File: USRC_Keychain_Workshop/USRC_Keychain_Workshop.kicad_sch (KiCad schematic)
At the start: 29 parts, among them U1 ICM7555xB, U2 4017

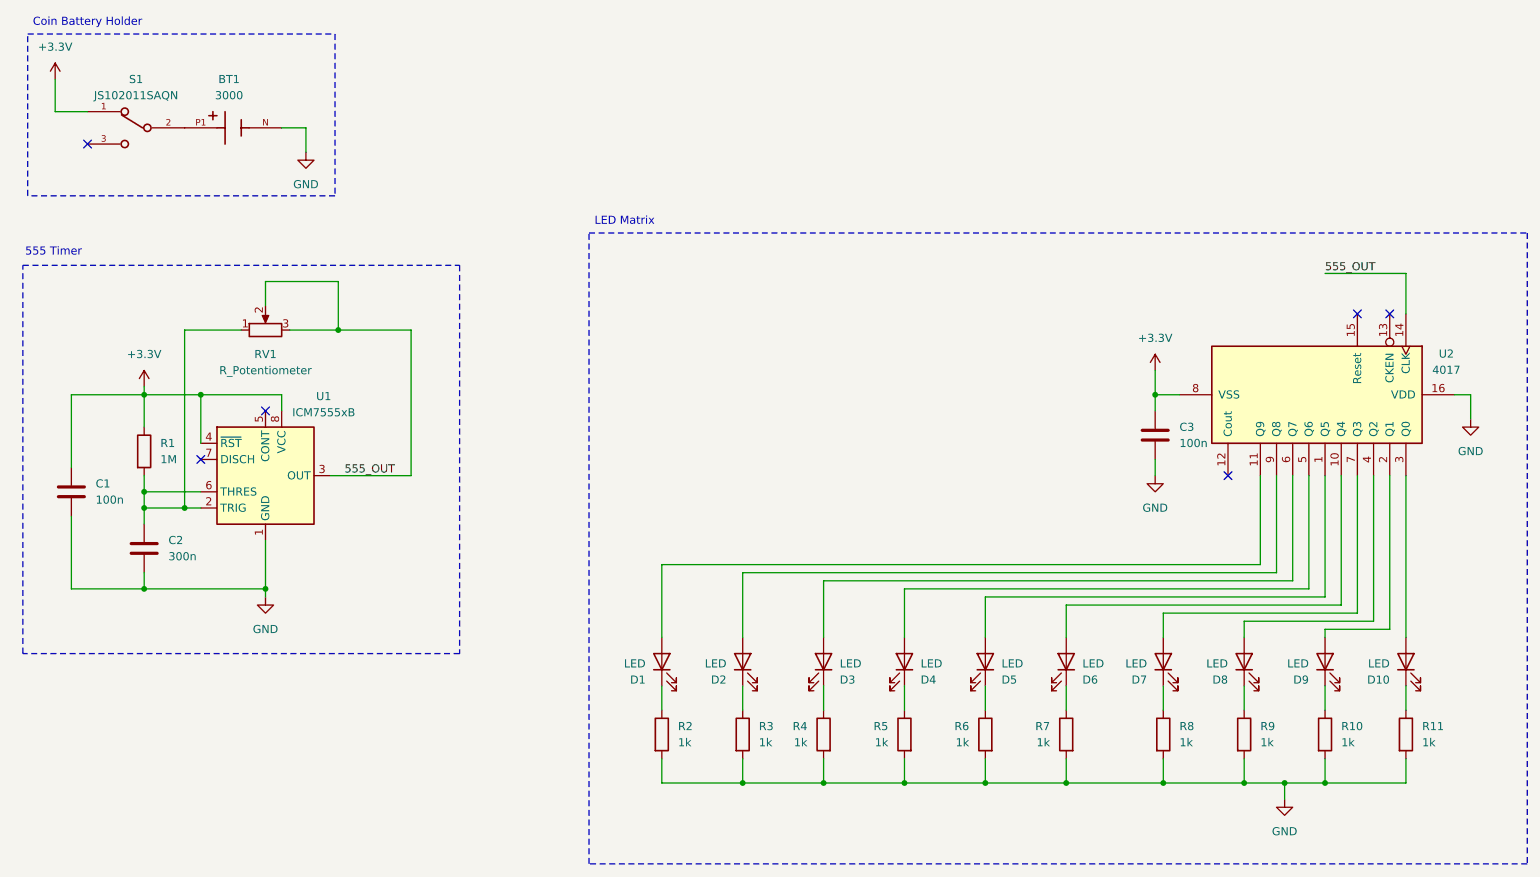
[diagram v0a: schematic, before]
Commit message: USRC_Keychain_Workshop version 2
Uploaded Version 2, a more trimmed down version of the KiCAD Keychain PCB Workshop, open the project from the KiCAD Project File.
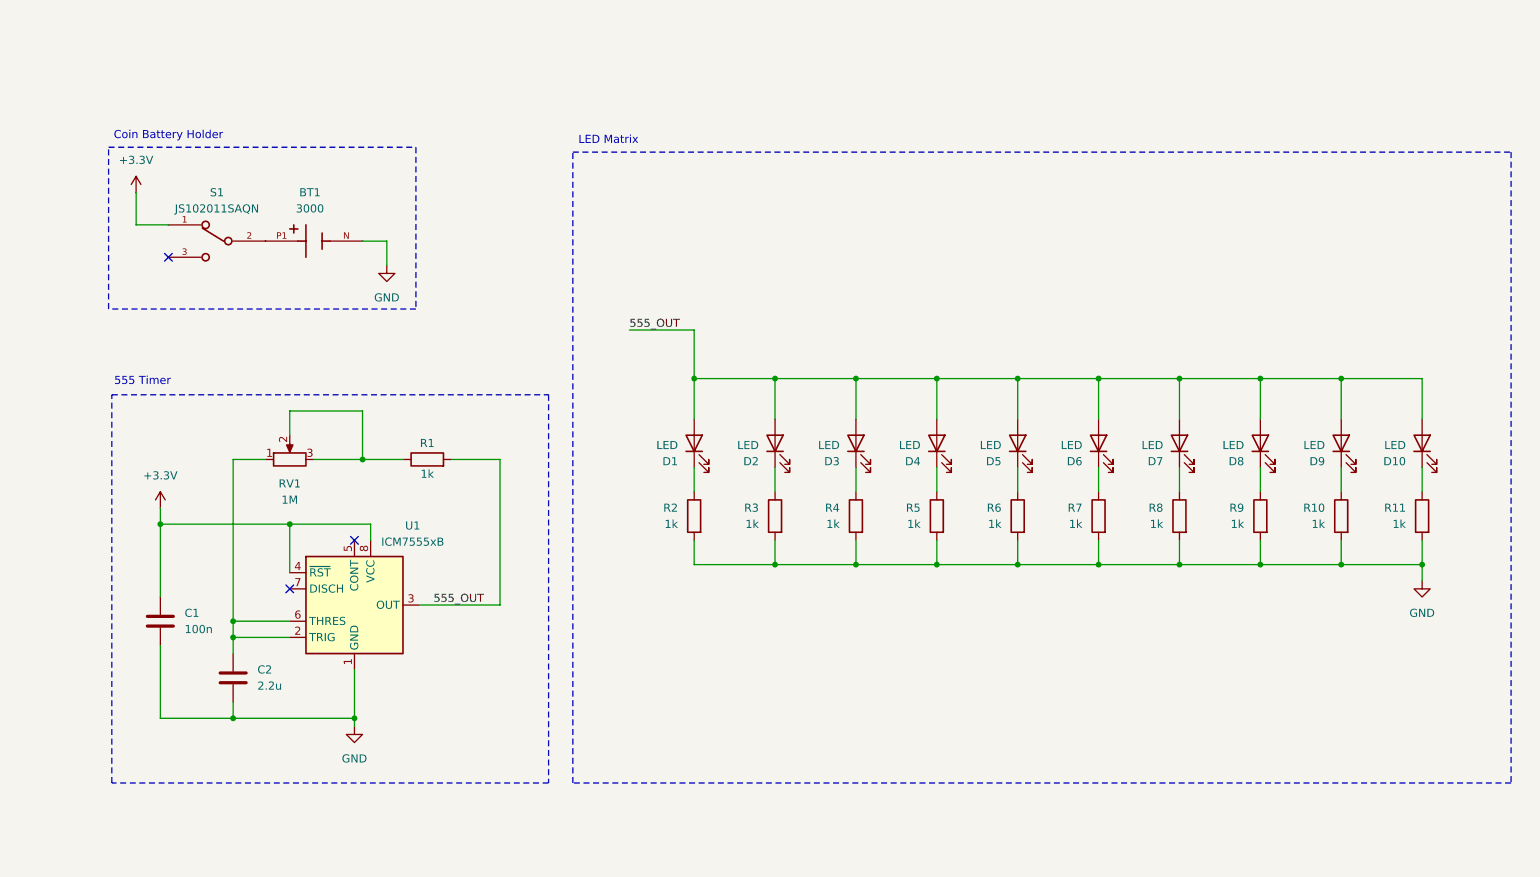
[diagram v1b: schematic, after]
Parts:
- removed C3: 100n, Capacitor_SMD:C_0805_2012Metric_Pad1.18x1.45mm_HandSolder, symbol Device:C
- removed U2: 4017, Package_DIP:DIP-16_W8.89mm_SMDSocket_LongPads, symbol 4xxx:4017
- C2: value 300n -> 2.2u
- R1: value 1M -> 1k
- RV1: value R_Potentiometer -> 1M
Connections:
- net +3.3V: no longer R1.1
- net 555_OUT: now also D1.2 (A), D10.2 (A), D2.2 (A), D3.2 (A), D4.2 (A), D5.2 (A), D6.2 (A), D7.2 (A), D8.2 (A), D9.2 (A), R1.2; no longer RV1.2, RV1.3
- net at C2.1, RV1.1, U1.2 (TRIG)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: no longer R1.2
- new net: R1.1, RV1.2, RV1.3
- no-connect marks 6 -> 3
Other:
- moved on the sheet: BT1, C1, C2, D1, D10, D2, D3, D4, D5, D6, D7, D8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
